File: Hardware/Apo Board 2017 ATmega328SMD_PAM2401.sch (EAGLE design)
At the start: 40 parts, among them Q1 RESONATORSMD, U1 PAM2401, U10 LED-TRICOLOR-5050-IC, U11 LED-TRICOLOR-5050-IC, U13 ATMEGA328, U2 LED-TRICOLOR-5050-IC, U3 LED-TRICOLOR-5050-IC, U4 LED-TRICOLOR-5050-IC, U5 LED-TRICOLOR-5050-IC, U6 LED-TRICOLOR-5050-IC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

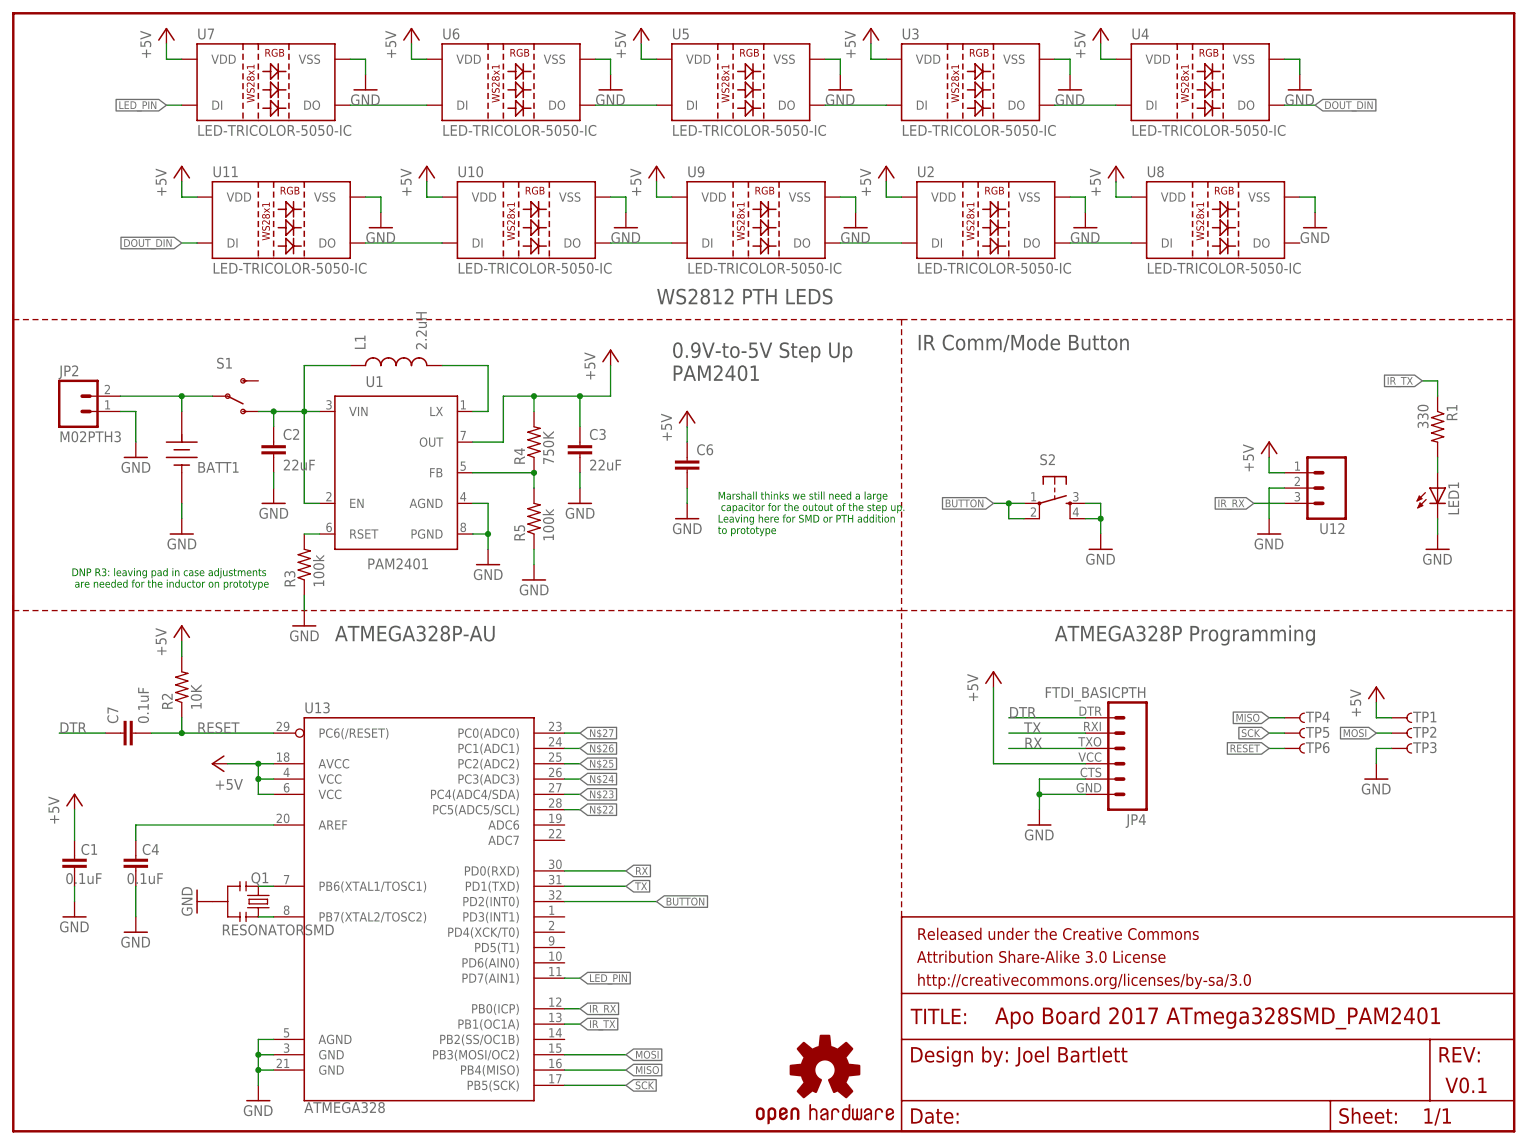
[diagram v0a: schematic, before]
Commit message: V0.2 Prototype and GERBERS
Added Kit footprints, updated silk, charged mounting holes, Named
board, added year,
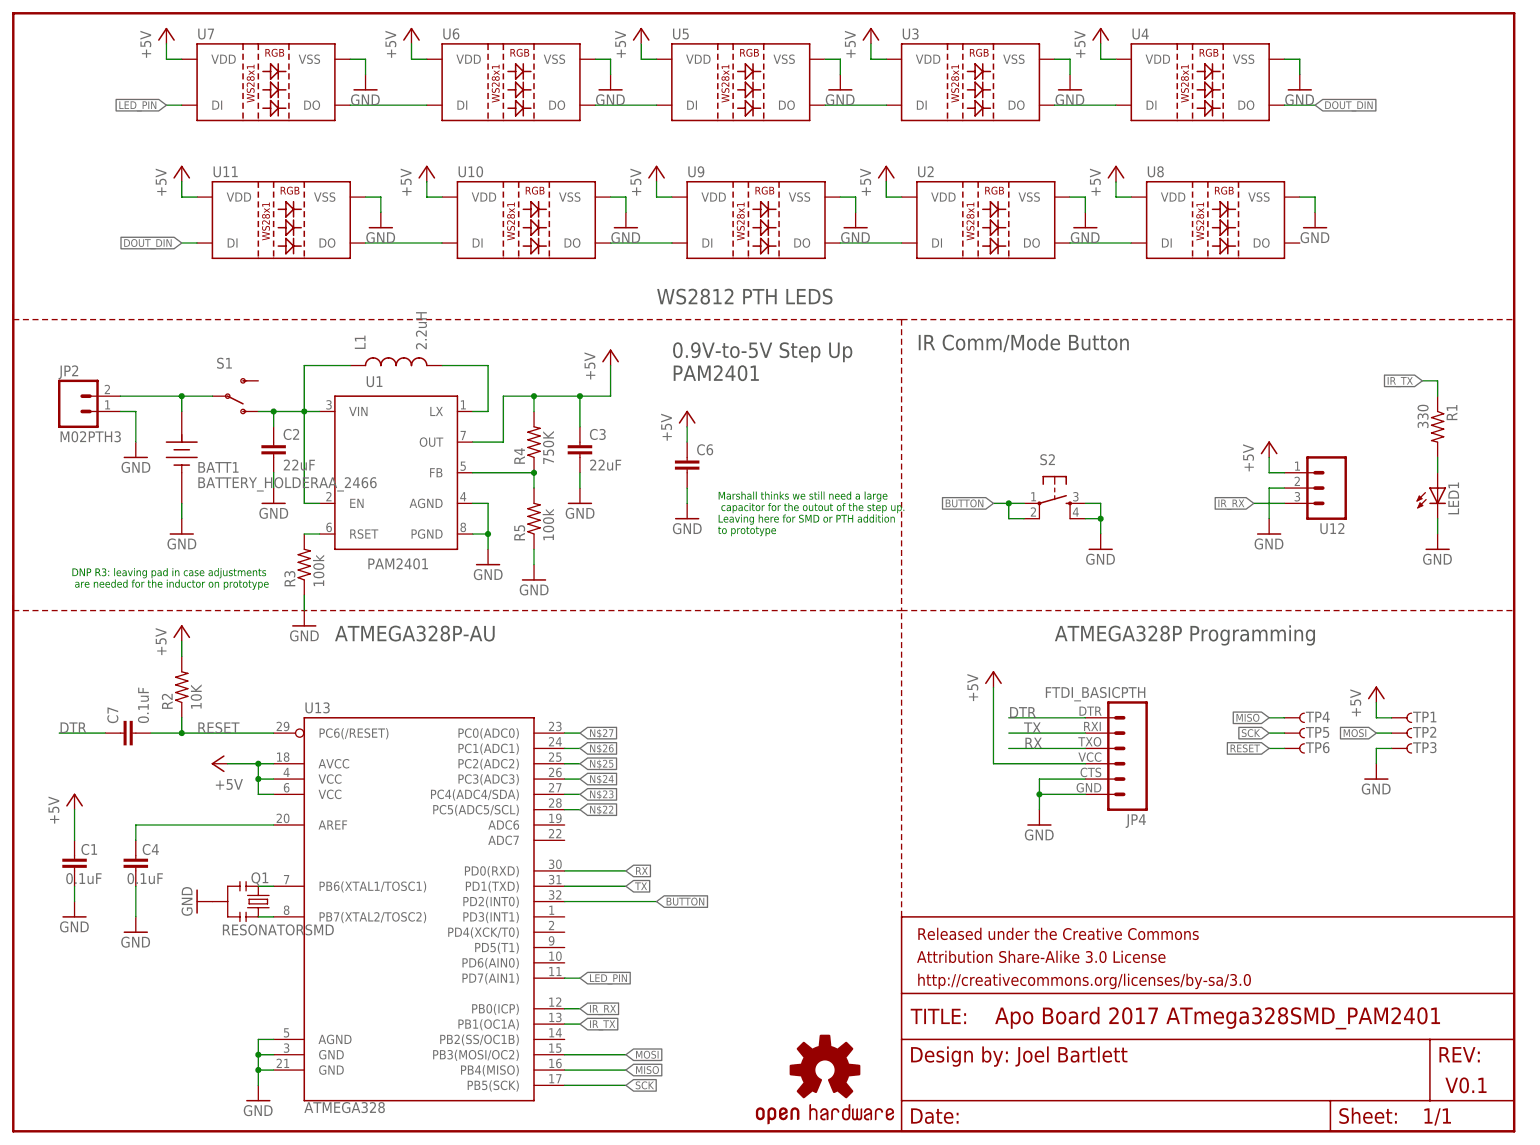
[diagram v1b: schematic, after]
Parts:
- LED1: device SparkFun-LED:LED5MM -> SparkFun-LED:LED5MM-KIT
- R1: device SparkFun-Resistors:RESISTORPTH-1/4W -> SparkFun-Resistors:RESISTORKIT
- U10, U11, U2, U3, U4, U5, U6, U7, U8, U9: value LED-TRICOLOR-5050-IC -> LED-TRICOLOR-5050-ICWS2812-THRU-KIT; device SparkFun-LED:LED-TRICOLOR-5050-IC -> SparkFun-LED:LED-TRICOLOR-5050-ICWS2812-THRU-KIT
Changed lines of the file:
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@@
 <?xml version="1.0" encoding="utf-8"?>
 <!DOCTYPE eagle SYSTEM "eagle.dtd">
-<eagle version="7.7.0">
+<eagle version="7.3.0">
 <drawing>
 <settings>
@@
 <setting verticaltext="up"/>
 </settings>
-<grid distance="0.05" unitdist="inch" unit="inch" style="lines" multiple="1" display="yes" altdistance="0.005" altunitdist="inch" altunit="inch"/>
+<grid distance="0.1" unitdist="inch" unit="inch" style="lines" multiple="1" display="no" altdistance="0.01" altunitdist="inch" altunit="inch"/>
 <layers>
 <layer number="1" name="Top" color="4" fill="1" visible="no" active="no"/>
@@
 </classes>
 <parts>
-<part name="U3" library="SparkFun-LED" deviceset="LED-TRICOLOR-5050-IC" device=""/>
-<part name="U4" library="SparkFun-LED" deviceset="LED-TRICOLOR-5050-IC" device=""/>
-<part name="U5" library="SparkFun-LED" deviceset="LED-TRICOLOR-5050-IC" device=""/>
-<part name="U6" library="SparkFun-LED" deviceset="LED-TRICOLOR-5050-IC" device=""/>
-<part name="U7" library="SparkFun-LED" deviceset="LED-TRICOLOR-5050-IC" device=""/>
+<part name="U3" library="SparkFun-LED" deviceset="LED-TRICOLOR-5050-IC" device="WS2812-THRU-KIT" value=""/>
+<part name="U4" library="SparkFun-LED" deviceset="LED-TRICOLOR-5050-IC" device="WS2812-THRU-KIT" value=""/>
+<part name="U5" library="SparkFun-LED" deviceset="LED-TRICOLOR-5050-IC" device="WS2812-THRU-KIT" value=""/>
+<part name="U6" library="SparkFun-LED" deviceset="LED-TRICOLOR-5050-IC" device="WS2812-THRU-KIT" value=""/>
+<part name="U7" library="SparkFun-LED" deviceset="LED-TRICOLOR-5050-IC" device="WS2812-THRU-KIT" value=""/>
 <part name="GND1" library="SparkFun-Aesthetics" deviceset="GND" device=""/>
 <part name="GND2" library="SparkFun-Aesthetics" deviceset="GND" device=""/>
@@
 <part name="S2" library="SparkFun-Electromechanical" deviceset="TAC_SWITCH" device="PTH"/>
 <part name="LOGO1" library="SparkFun-Aesthetics" deviceset="OSHW-LOGO" device="S"/>
-<part name="LED1" library="SparkFun-LED" deviceset="LED" device="5MM"/>
-<part name="R1" library="SparkFun-Resistors" deviceset="RESISTOR" device="PTH-1/4W" value="330"/>
+<part name="LED1" library="SparkFun-LED" deviceset="LED" device="5MM-KIT"/>
+<part name="R1" library="SparkFun-Resistors" deviceset="RESISTOR" device="KIT" value="330"/>
 <part name="P+6" library="supply1" deviceset="+5V" device=""/>
 <part name="P+7" library="supply1" deviceset="+5V" device=""/>
 <part name="GND15" library="supply1" deviceset="GND" device=""/>
 <part name="JP4" library="SparkFun-Connectors" deviceset="FTDI_BASIC" device="PTH"/>
-<part name="U2" library="SparkFun-LED" deviceset="LED-TRICOLOR-5050-IC" device=""/>
-<part name="U8" library="SparkFun-LED" deviceset="LED-TRICOLOR-5050-IC" device=""/>
-<part name="U9" library="SparkFun-LED" deviceset="LED-TRICOLOR-5050-IC" device=""/>
-<part name="U10" library="SparkFun-LED" deviceset="LED-TRICOLOR-5050-IC" device=""/>
-<part name="U11" library="SparkFun-LED" deviceset="LED-TRICOLOR-5050-IC" device=""/>
+<part name="U2" library="SparkFun-LED" deviceset="LED-TRICOLOR-5050-IC" device="WS2812-THRU-KIT" value=""/>
+<part name="U8" library="SparkFun-LED" deviceset="LED-TRICOLOR-5050-IC" device="WS2812-THRU-KIT" value=""/>
+<part name="U9" library="SparkFun-LED" deviceset="LED-TRICOLOR-5050-IC" device="WS2812-THRU-KIT" value=""/>
+<part name="U10" library="SparkFun-LED" deviceset="LED-TRICOLOR-5050-IC" device="WS2812-THRU-KIT" value=""/>
+<part name="U11" library="SparkFun-LED" deviceset="LED-TRICOLOR-5050-IC" device="WS2812-THRU-KIT" value=""/>
 <part name="GND6" library="SparkFun-Aesthetics" deviceset="GND" device=""/>
 <part name="GND12" library="SparkFun-Aesthetics" deviceset="GND" device=""/>
@@
 <part name="GND11" library="SparkFun" deviceset="GND" device=""/>
 <part name="GND14" library="SparkFun" deviceset="GND" device=""/>
-<part name="BATT1" library="1_BES_ELECTROMECHANICAL" deviceset="BATTERY_HOLDER" device="AA_2466" value=""/>
+<part name="BATT1" library="1_BES_ELECTROMECHANICAL" deviceset="BATTERY_HOLDER" device="AA_2466" value="BATTERY_HOLDERAA_2466"/>
 <part name="JP2" library="SparkFun-Connectors" deviceset="M02" device="PTH3"/>
 <part name="GND17" library="SparkFun" deviceset="GND" device=""/>
